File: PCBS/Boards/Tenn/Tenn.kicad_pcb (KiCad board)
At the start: 2 copper layers, 85.5 x 24 mm, 66 parts, among them J1 Conn_01x02_Socket, J15 Conn_01x03_Male, J16 Conn_01x02_Male, J17 Conn_01x02_Male, J18 Conn_01x30_Pin, SW2 SW_Push, SW3 SW_Push, SW4 SW_SPDT, U2 DRV8871DDA, U3 DRV8871DDA

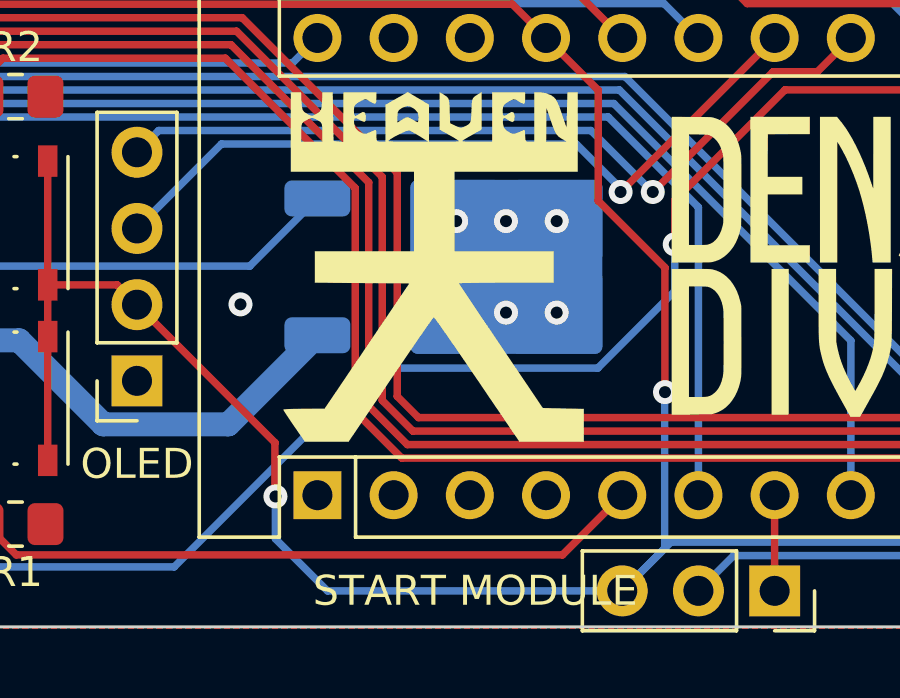
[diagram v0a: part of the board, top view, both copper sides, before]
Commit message: updates files on tenn pcb, fixes error with GND not being connected
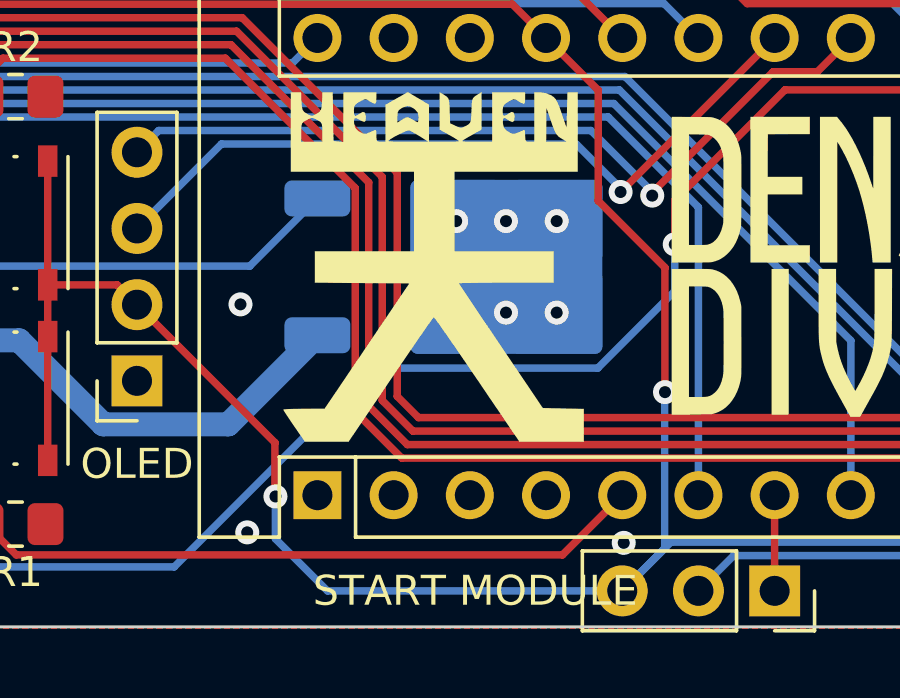
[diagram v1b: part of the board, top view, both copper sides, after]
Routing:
- net GND: vias 8 -> 10
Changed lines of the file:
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@@
+		)
+	)
+	(gr_text "SENS2\n"
+		(at 128.956 86.4 90)
+		(layer "Cmts.User")
+		(effects
+			(font
+				(size 1.5 1.5)
+				(thickness 0.3)
+				(bold yes)
+			)
+			(justify left bottom)
 		)
 	)
@@
 		)
 	)
-	(gr_text "SENS2\n"
-		(at 128.956 86.4 90)
-		(layer "Edge.Cuts")
-		(effects
-			(font
-				(size 1.5 1.5)
-				(thickness 0.3)
-				(bold yes)
-			)
-			(justify left bottom)
-		)
-	)
 	(dimension
 		(type aligned)
@@
 	)
 	(via
+		(at 155.95 108.2)
+		(size 0.8)
+		(drill 0.4)
+		(layers "F.Cu" "B.Cu")
+		(free yes)
+		(net 4)
+	)
+	(via
 		(at 150.365 97.475)
 		(size 0.8)
@@
 	(via
 		(at 143.175 100.25)
+		(size 0.8)
+		(drill 0.4)
+		(layers "F.Cu" "B.Cu")
+		(free yes)
+		(net 4)
+	)
+	(via
+		(at 143.4 107.85)
 		(size 0.8)
 		(drill 0.4)
@@
 	)
 	(via
-		(at 156.917922 96.504623)
-		(size 0.8)
-		(drill 0.4)
+		(at 156.9 96.625)
+		(size 0.8)
+		(drill 0.4)

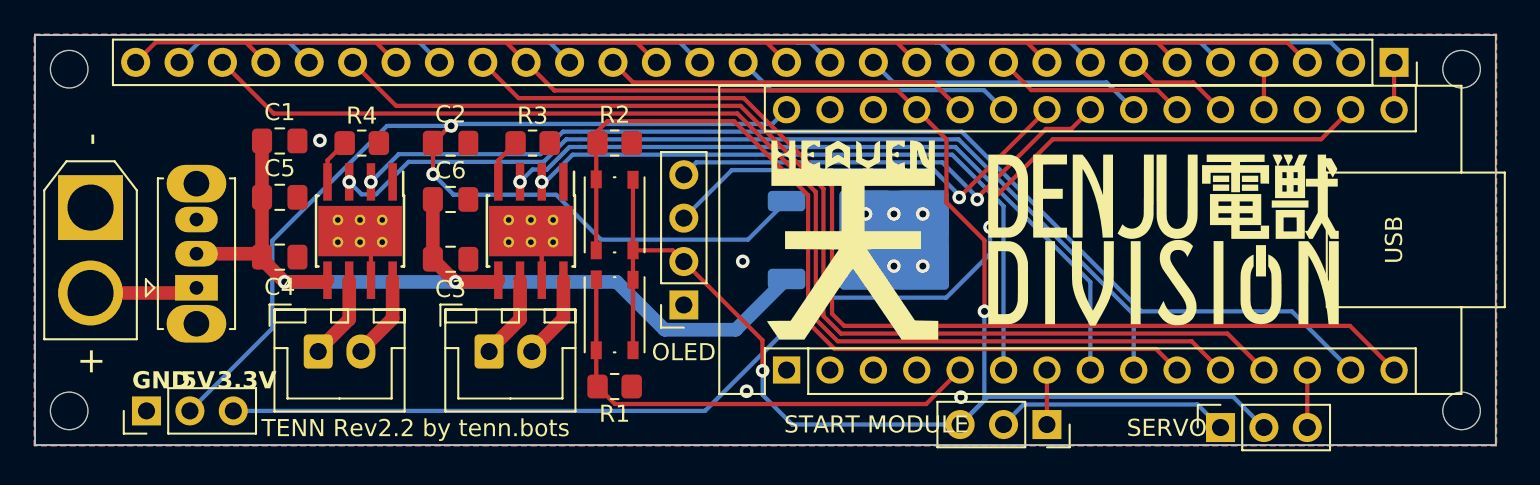
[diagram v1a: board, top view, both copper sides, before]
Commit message: updates files of tenn pcb, changes foot print of 47uf capacitor, fixes unconnected vias and traces, adds Arduino GPIO references in the backside for easier understanding of the board
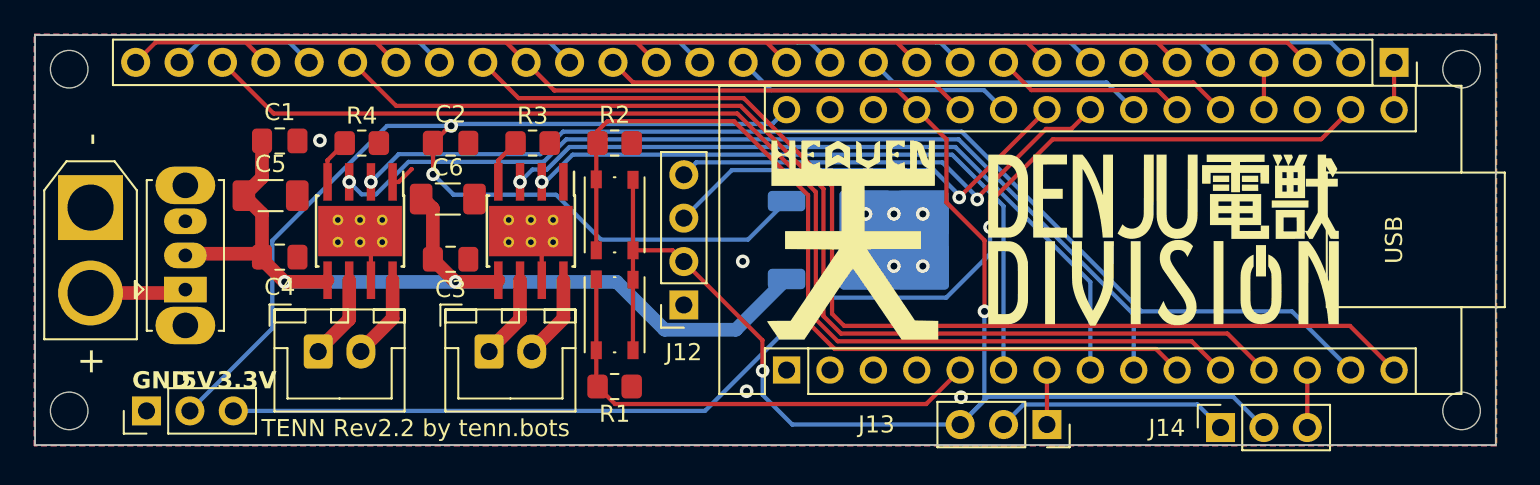
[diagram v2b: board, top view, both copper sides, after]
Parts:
- C5, C6: footprint Capacitor_SMD:C_0805_2012Metric_Pad1.18x1.45mm_HandSolder -> Capacitor_SMD:C_1206_3216Metric_Pad1.33x1.80mm_HandSolder
- J13: renamed from START MODULE
- moved SW4 0.66 mm to (110.5, 101.9)
- moved C5 0.55 mm to (115.5, 96.4)
- moved C6 0.16 mm to (125.9, 96.6)
- renumbered OLED to J12, SERVO to J14, L7805/BEC to U1
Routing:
- net VM: track 55.2 -> 57.1 mm
- net GND: track 102.8 -> 104.2 mm
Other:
- board text added: "A0"
- board text added: "A1"
- board text added: "A2"
- board text added: "A3"
- board text added: "A6"
- board text added: "A7"
- board text added: "D12"
- board text added: "D13"
- board text added: "D8"
- board text added: "D9"
